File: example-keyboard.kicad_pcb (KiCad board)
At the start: 2 copper layers, 10 parts, among them SW1 SW_Push, U1 Elite-C

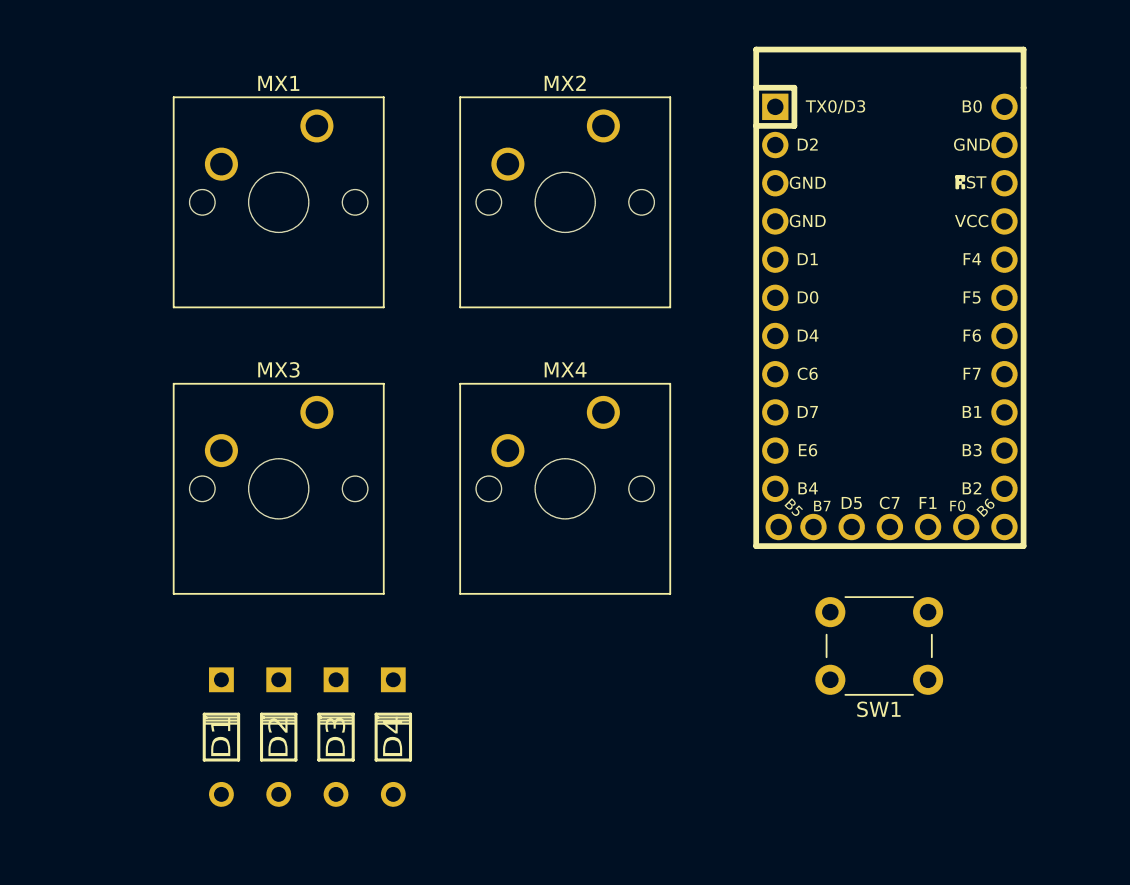
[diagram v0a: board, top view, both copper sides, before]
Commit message: Adds edge cuts
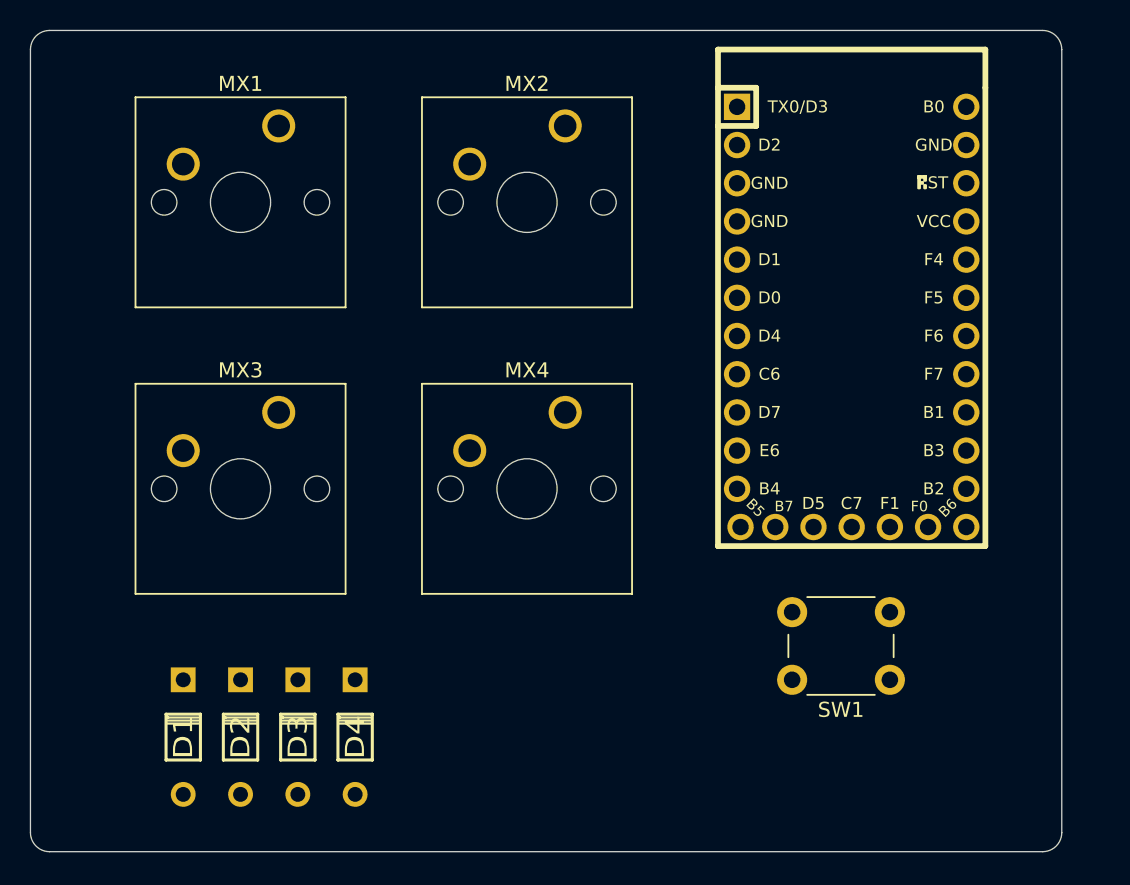
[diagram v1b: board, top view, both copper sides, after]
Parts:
- moved D1 2.54 mm to (73.7, 94.0)
- moved D2 2.54 mm to (77.5, 94.0)
- moved U1 2.54 mm to (118.1, 66.0)
- moved D3 2.54 mm to (81.3, 94.0)
- moved D4 2.54 mm to (85.1, 94.0)
- moved MX1 2.54 mm to (80.0, 53.3)
- moved MX2 2.54 mm to (99.1, 53.3)
- moved MX3 2.54 mm to (80.0, 72.4)
- moved MX4 2.54 mm to (99.1, 72.4)
- moved SW1 2.54 mm to (120.7, 90.2)
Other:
- board outline added: 68.6 x 54.6 mm

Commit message: better layout
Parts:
- moved D4 12.8 mm to (97.8, 92.7)
- moved D3 11.5 mm to (92.7, 95.2)
- moved SW1 7.62 mm to (120.7, 97.8)
- moved D2 1.80 mm to (78.7, 92.7)
- moved D1 1.27 mm to (73.7, 95.2)
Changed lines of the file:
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@@
   )
   (module Button_Switch_THT:SW_PUSH_6mm_H7.3mm (layer F.Cu)
-    (at 120.65 90.17 180)
+    (at 120.65 97.79 180)
     (descr "tactile push button, 6x6mm e.g. PHAP33xx series, height=7.3mm")
     (tags "tact sw push 6mm")
@@
   )
   (module Keebio-Parts:Diode (layer F.Cu)
-    (at 85.09 93.98 90)
+    (at 97.79 92.71 90)
     (fp_text reference D4 (at 0 0 90) (layer F.SilkS)
       (effects (font (size 1.27 1.524) (thickness 0.2032)))
@@
   )
   (module Keebio-Parts:Diode (layer F.Cu)
-    (at 81.28 93.98 90)
+    (at 92.71 95.25 90)
     (fp_text reference D3 (at 0 0 90) (layer F.SilkS)
       (effects (font (size 1.27 1.524) (thickness 0.2032)))
@@
   )
   (module Keebio-Parts:Diode (layer F.Cu)
-    (at 77.47 93.98 90)
+    (at 78.74 92.71 90)
     (fp_text reference D2 (at 0 0 90) (layer F.SilkS)
       (effects (font (size 1.27 1.524) (thickness 0.2032)))
@@
   )
   (module Keebio-Parts:Diode (layer F.Cu)
-    (at 73.66 93.98 90)
+    (at 73.66 95.25 90)
     (fp_text reference D1 (at 0 0 90) (layer F.SilkS)
       (effects (font (size 1.27 1.524) (thickness 0.2032)))

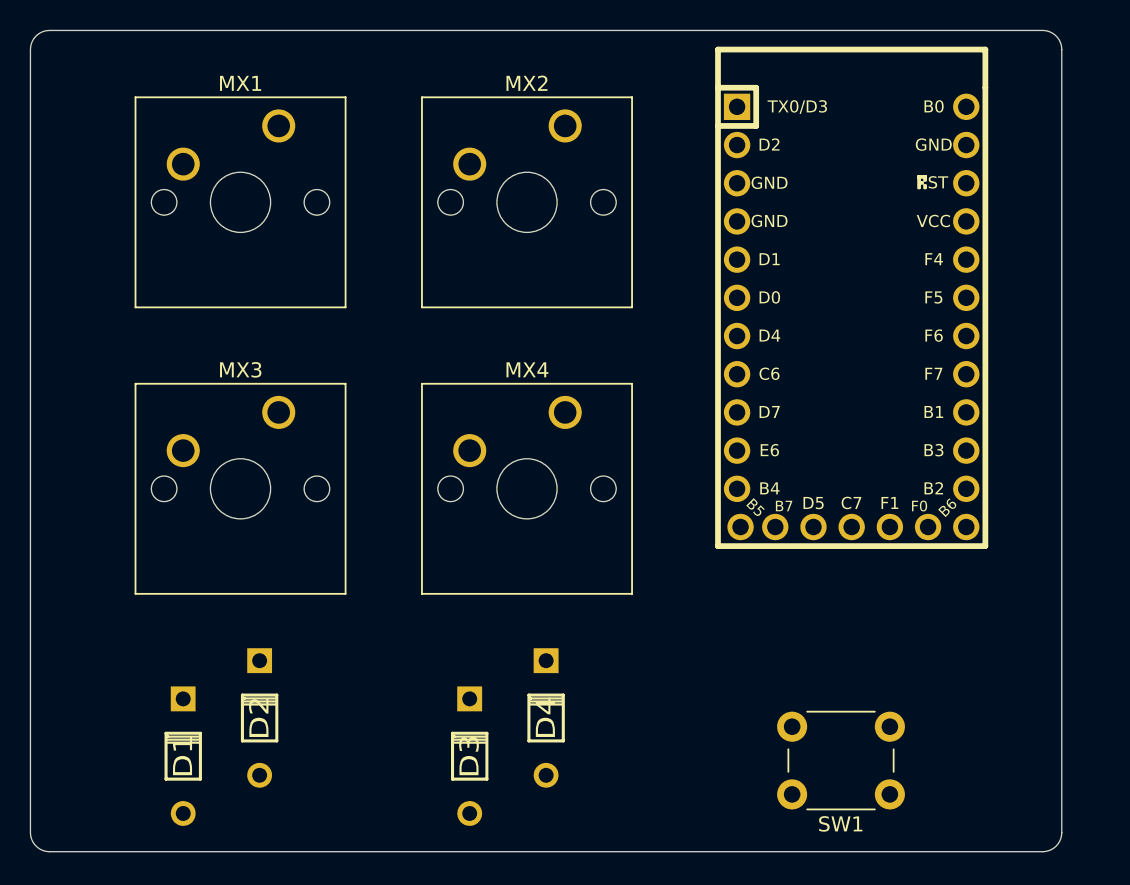
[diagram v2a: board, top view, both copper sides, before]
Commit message: Adds routing that I think works but I changed the pins that the rows/columns are talking to so that may bite me
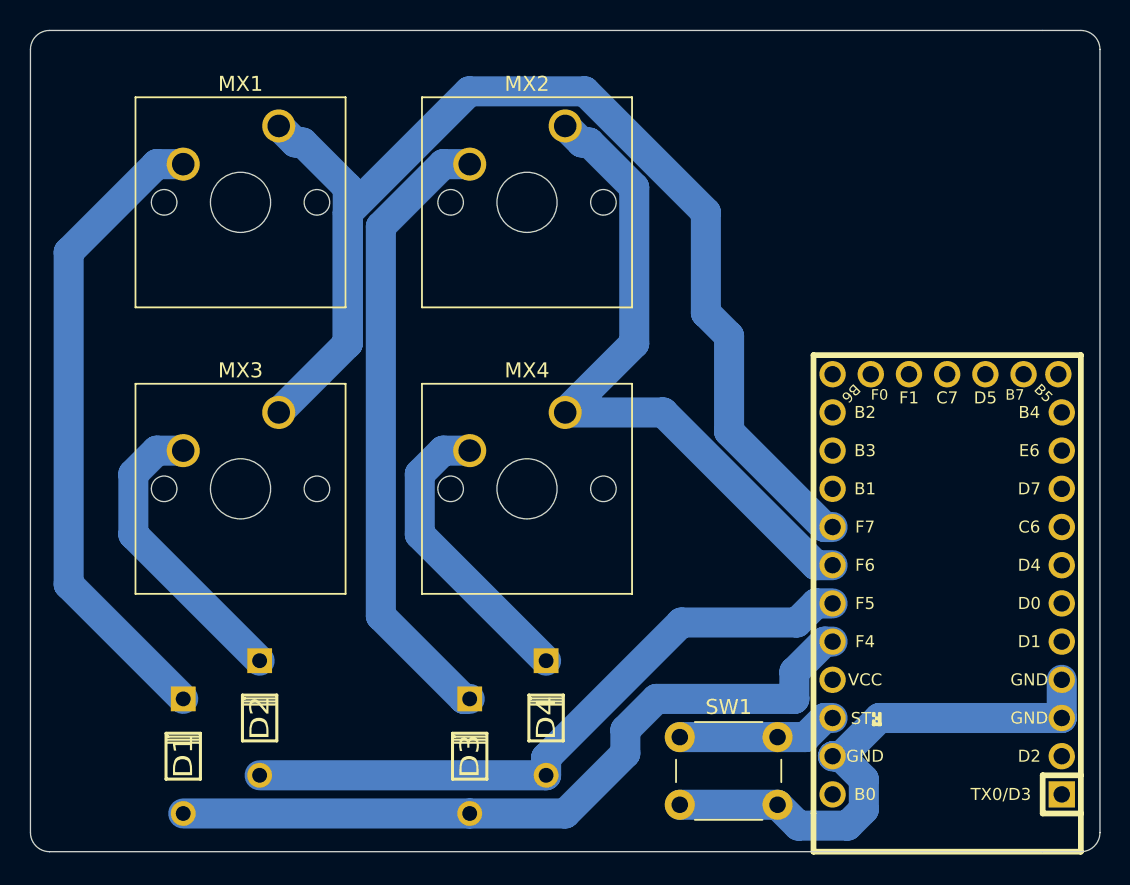
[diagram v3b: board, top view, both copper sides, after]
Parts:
- moved U1 18.9 mm to (124.5, 83.8), turned to 90 degrees
- moved SW1 14.5 mm to (106.7, 94.0), turned to 0 degrees
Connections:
- U1 pad 17: Net-(U1-Pad17) -> ROW1
- U1 pad 18: Net-(U1-Pad18) -> ROW2
- U1 pad 2: COL1 -> Net-(U1-Pad2)
- U1 pad 20: Net-(U1-Pad20) -> COL1
- U1 pad 7: ROW1 -> Net-(U1-Pad7)
- U1 pad 9: ROW2 -> Net-(U1-Pad9)
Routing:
- net ROW1: track 0.00 -> 87.0 mm
- net COL1: track 0.00 -> 49.9 mm
- net ROW2: track 0.00 -> 45.1 mm
- net COL2: track 0.00 -> 43.5 mm
- net Net-(D1-Pad2): track 0.00 -> 42.9 mm
- net Net-(D3-Pad2): track 0.00 -> 41.7 mm
- net GND: track 0.00 -> 36.7 mm
- net Net-(D4-Pad2): track 0.00 -> 19.9 mm
- net Net-(D2-Pad2): track 0.00 -> 19.9 mm
- net Net-(SW1-Pad1): track 0.00 -> 10.7 mm
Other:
- board size 68.6 x 54.6 mm -> 71.1 x 54.6 mm
- net class Default: trace_width 0.25 -> 2

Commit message: Adds logo (who knew it would be this difficult to make an svg look good on a board)
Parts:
- added Ref**: Val**, keyboards:arny-kicad-test-final, F.Cu at (124.5, 57.1)
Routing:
- added copper zone on B.Cu, net GND
